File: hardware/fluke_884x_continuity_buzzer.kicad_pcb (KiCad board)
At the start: 4 copper layers, 67.4 x 71.4 mm, 70 parts, among them J2 Conn_01x02, J203 16 pin DIP socket, J204 16 pin DIP socket, J3 USB_B_Micro, P203 16 pin DIP plug, P204 16 pin DIP plug, U1 AZ117EH-3.3, U2 W25Q128JVS, U3 RP2040, Y1 ABLS-12.000MHZ-B4-T

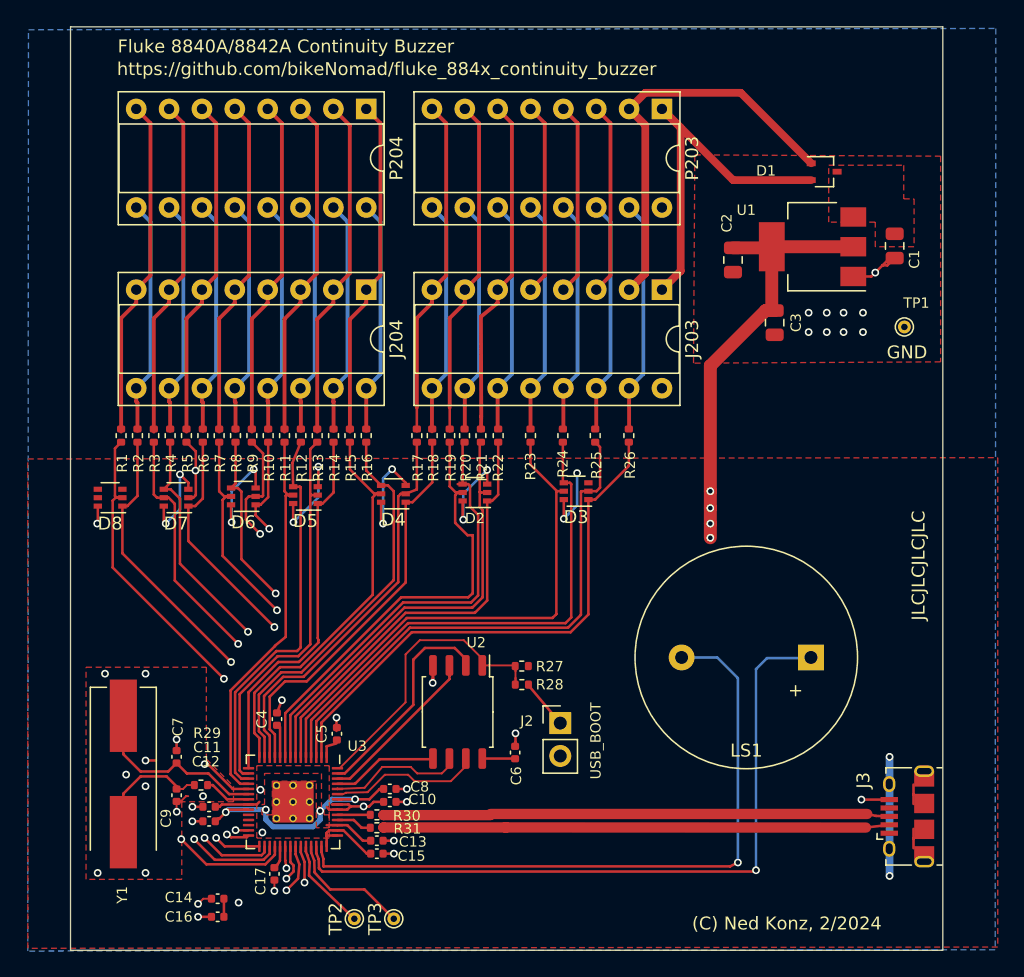
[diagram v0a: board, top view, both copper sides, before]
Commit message: WIP: made board shorter
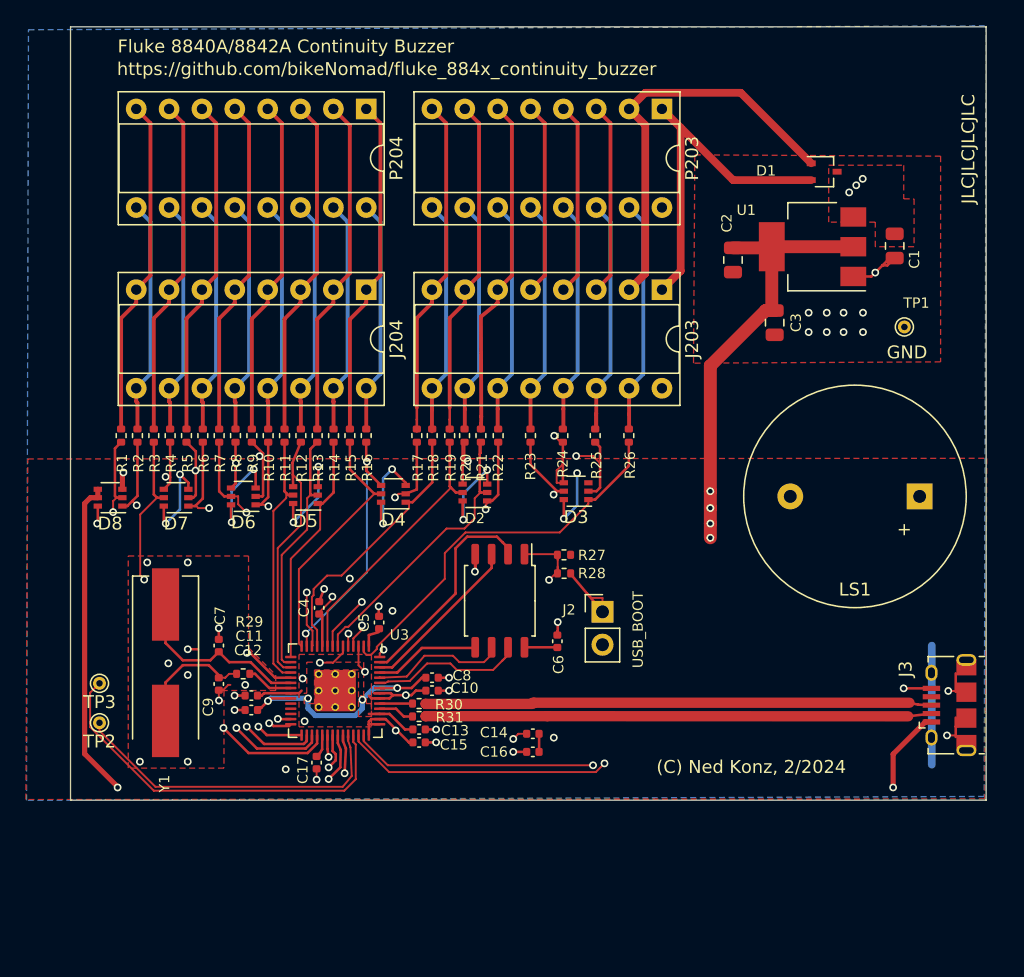
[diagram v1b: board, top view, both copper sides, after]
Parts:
- moved TP3 29.1 mm to (75.9, 76.2), turned to 180 degrees
- moved C14 27.5 mm to (109.4, 80.0)
- moved C16 27.5 mm to (109.4, 81.5)
- moved TP2 24.9 mm to (75.9, 79.2), turned to 180 degrees
- moved LS1 15.0 mm to (134.3, 61.7)
- moved C4 9.20 mm to (92.9, 70.3)
- moved Y1 9.20 mm to (81.0, 74.6)
- moved J2 9.20 mm to (114.8, 70.6)
- moved R29 9.20 mm to (87.0, 75.4)
- moved C10 9.20 mm to (101.6, 76.7)
- moved C11 9.20 mm to (87.6, 77.1)
- moved C12 9.20 mm to (87.6, 78.2)
- moved C13 9.20 mm to (100.6, 79.7)
- moved C15 9.20 mm to (100.6, 80.7)
- moved C17 9.20 mm to (92.7, 82.3)
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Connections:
- D8 pad 3: unconnected-(D8C-K-Pad3) -> Net-(D1-K)
- D8 pad 4: unconnected-(D8C-A-Pad4) -> /VBUS
- D8 pad 5: unconnected-(D8D-A-Pad5) -> /VBUS
- J3 pad 1: unconnected-(J3-VBUS-Pad1) -> /VBUS
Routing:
- net /VBUS: track 0.00 -> 91.5 mm, vias 0 -> 2
- net Net-(D1-K): track 0.00 -> 82.2 mm, vias 0 -> 4
- net /GPIO27_ADC1: track 9.70 -> 30.1 mm
- net /GPIO26_ADC0: track 7.09 -> 25.5 mm
- net RL4_3V: track 40.4 -> 27.2 mm, vias 0 -> 2
- net G1_3V: track 46.5 -> 33.4 mm
- net G7_3V: track 35.4 -> 22.3 mm
- net PDP_3V: track 31.0 -> 19.6 mm
- net G5_3V: track 34.0 -> 22.7 mm
- net RL3_3V: track 41.7 -> 30.4 mm
- net G3_3V: track 29.1 -> 18.1 mm
- net PS1_3V: track 30.1 -> 19.3 mm
- net PS2_3V: track 46.2 -> 35.4 mm
- net RL1_3V: track 34.4 -> 23.7 mm, vias 0 -> 2
- net RL2_3V: track 40.3 -> 29.7 mm, vias 0 -> 2
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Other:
- board size 67.4 x 71.4 mm -> 70.8 x 59.8 mm

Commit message: WIP: shortened board, added driver for keypad signals.
Also changed 30V R values.
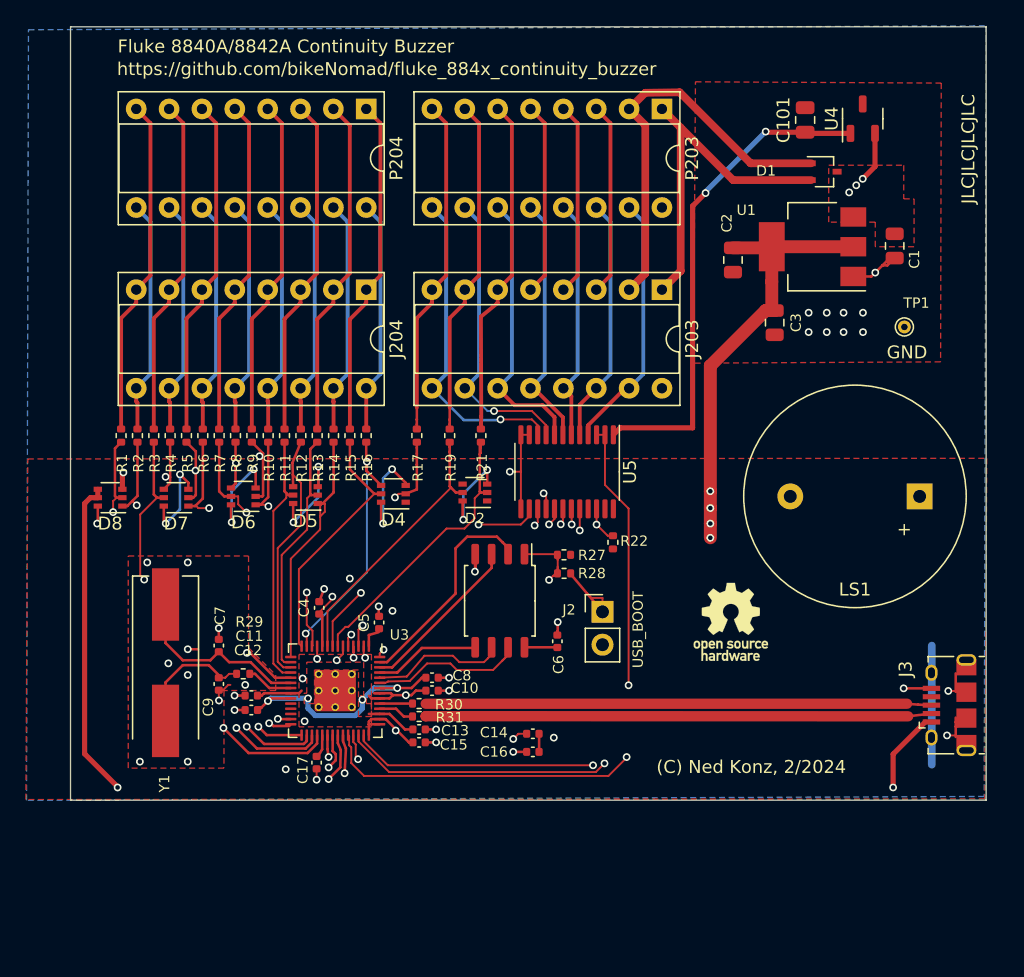
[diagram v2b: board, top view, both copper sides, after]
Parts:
- removed D3: BAT54CDW, Package_TO_SOT_SMD:SOT-363_SC-70-6
- removed R18, R20, R23, R24, R25, R26: 15k, Resistor_SMD:R_0402_1005Metric
- removed TP2, TP3: TestPoint, TestPoint:TestPoint_THTPad_D1.0mm_Drill0.5mm
- added C101: 10u, Capacitor_SMD:C_0805_2012Metric, F.Cu at (130.4, 32.6)
- added REF**: OSHW-Logo_5.7x6mm_SilkScreen, Symbol:OSHW-Logo_5.7x6mm_SilkScreen, F.Cu at (124.7, 71.4)
- added U4: umw_78l05_sot23, Package_TO_SOT_SMD:SOT-23-3, F.Cu at (134.9, 32.5)
- added U5: SN74LVC8T245PW, Package_SO:TSSOP-24_4.4x7.8mm_P0.65mm, F.Cu at (112.0, 59.8)
- R1, R10, R11, R12, R13, R14, R15, R16, R17, R19, R2, R21, R3, R4, R5, R6, R7, R8, R9: value 470k -> 270k
- R22: value 15k -> 10k
- moved R22 12.1 mm to (115.6, 65.2)
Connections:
- D2 pad 1: RL6_3V -> unconnected-(D2A-A-Pad1)
- D2 pad 4: RL1_3V -> unconnected-(D2C-A-Pad4)
- D4 pad 1: RL0_3V -> unconnected-(D4A-A-Pad1)
- R22 pad 1: /RL6 -> /GPIO27_ADC1
- R22 pad 2: RL6_3V -> +3V3
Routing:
- net +5V: track 0.00 -> 38.1 mm, vias 0 -> 2
- net /GPIO26_ADC0: track 25.5 -> 51.1 mm, vias 0 -> 2
- net RL5_3V: track 32.8 -> 22.3 mm
- net GND: track 57.2 -> 64.5 mm, vias 36 -> 37
- net RL2_3V: track 29.7 -> 22.9 mm
- net RL4_3V: track 27.2 -> 21.2 mm
- net RL3_3V: track 30.4 -> 24.6 mm, vias 0 -> 2
- net /RL0: track 19.7 -> 25.0 mm, vias 0 -> 1
- net Net-(D1-K): track 82.2 -> 86.1 mm
- net /RL1: track 19.7 -> 23.1 mm, vias 0 -> 1
- net +3V3: track 113.8 -> 110.9 mm, vias 25 -> 23
- net RL6_3V: track 27.4 -> 24.9 mm
- net /GPIO27_ADC1: track 30.1 -> 32.1 mm, vias 0 -> 2
- net /RL6: track 19.7 -> 21.6 mm
- net RL1_3V: track 23.7 -> 22.0 mm
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
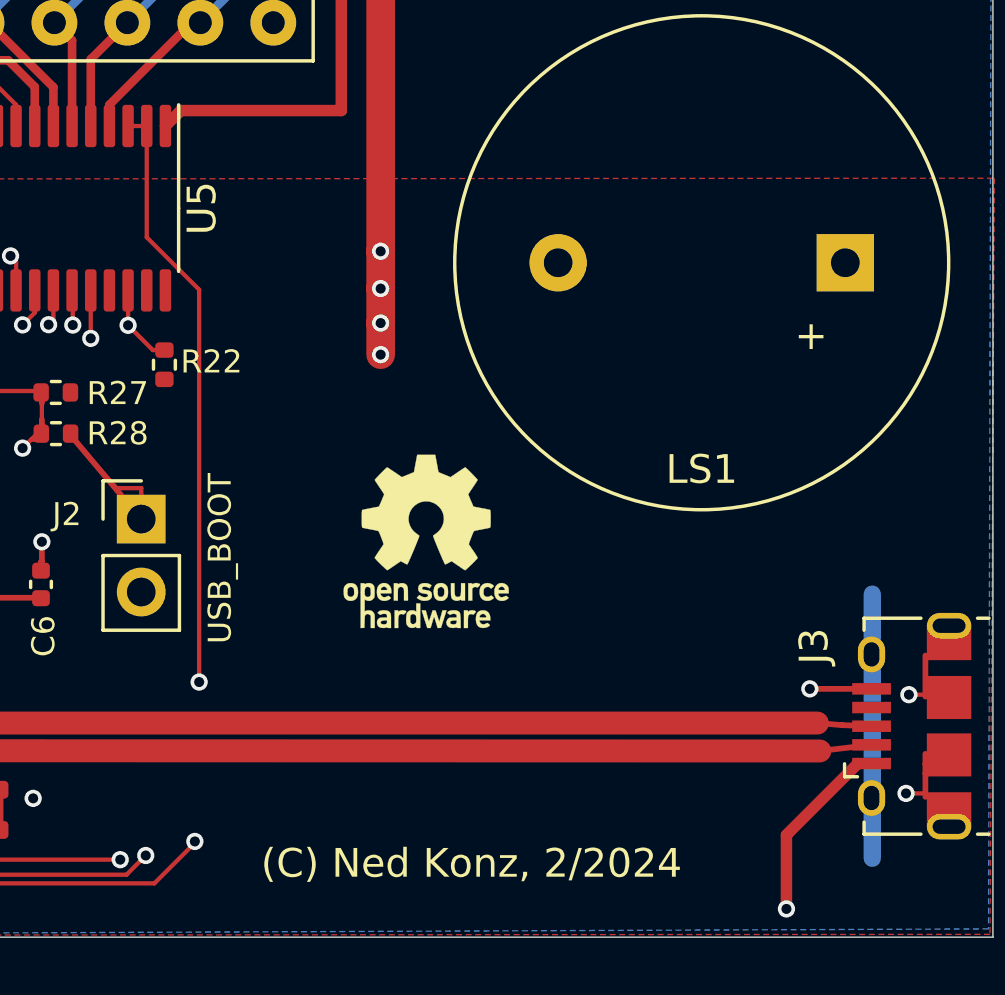
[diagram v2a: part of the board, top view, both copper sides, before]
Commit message: Added QR code; fixed JLC refs
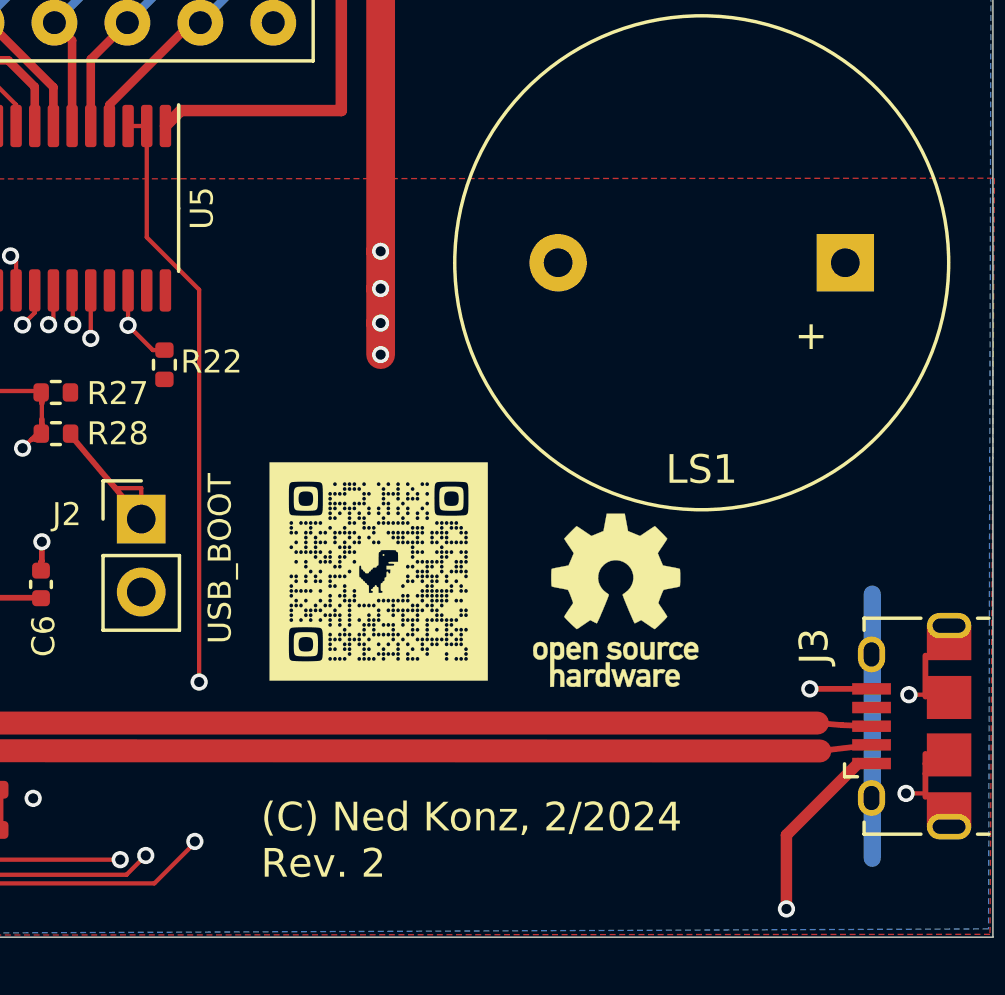
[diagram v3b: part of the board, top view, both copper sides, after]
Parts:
- added G***: LOGO, RP2040_minimal:qrcode, F.Cu at (123.0, 72.5)
- moved REF** 6.91 mm to (131.3, 73.5)
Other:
- board text added: "(C) Ned Konz, 2/2024 Rev. 2"
- board text removed: "(C) Ned Konz, 2/2024"

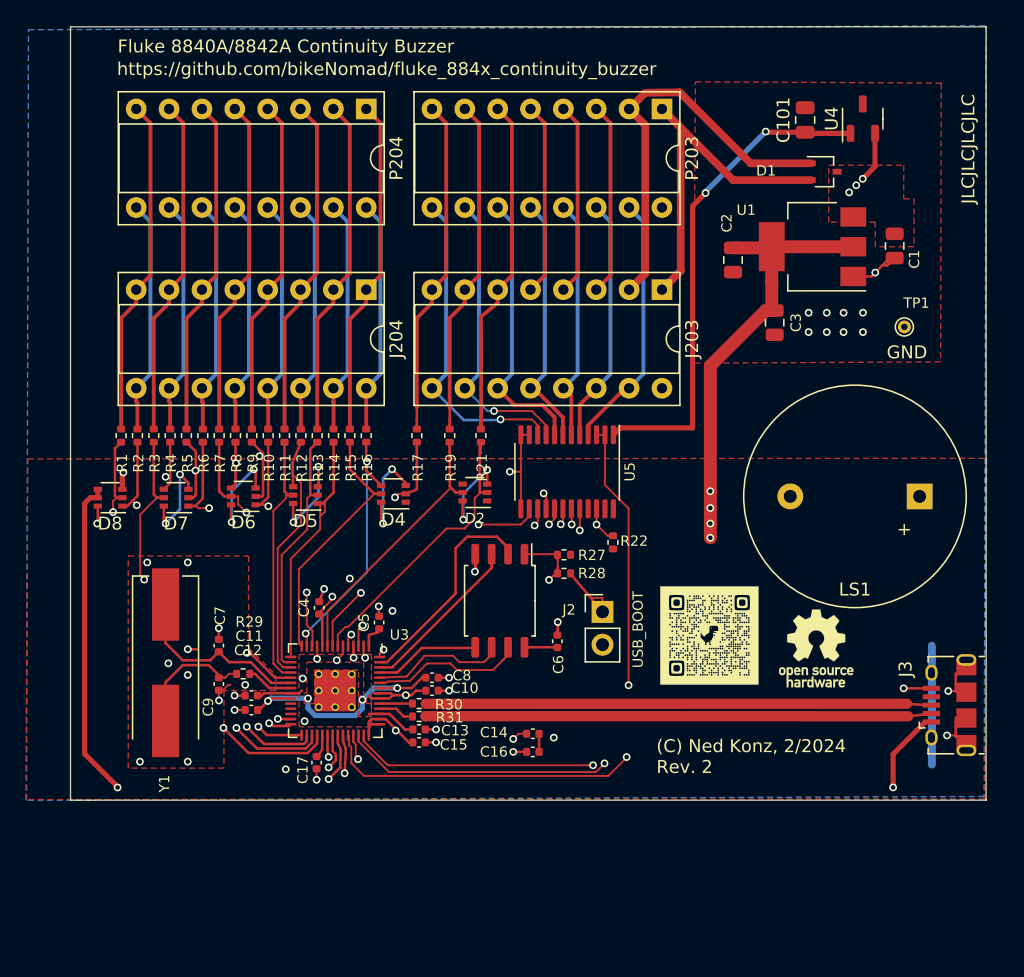
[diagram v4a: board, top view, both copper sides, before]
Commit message: Change R1-R19 to 200k
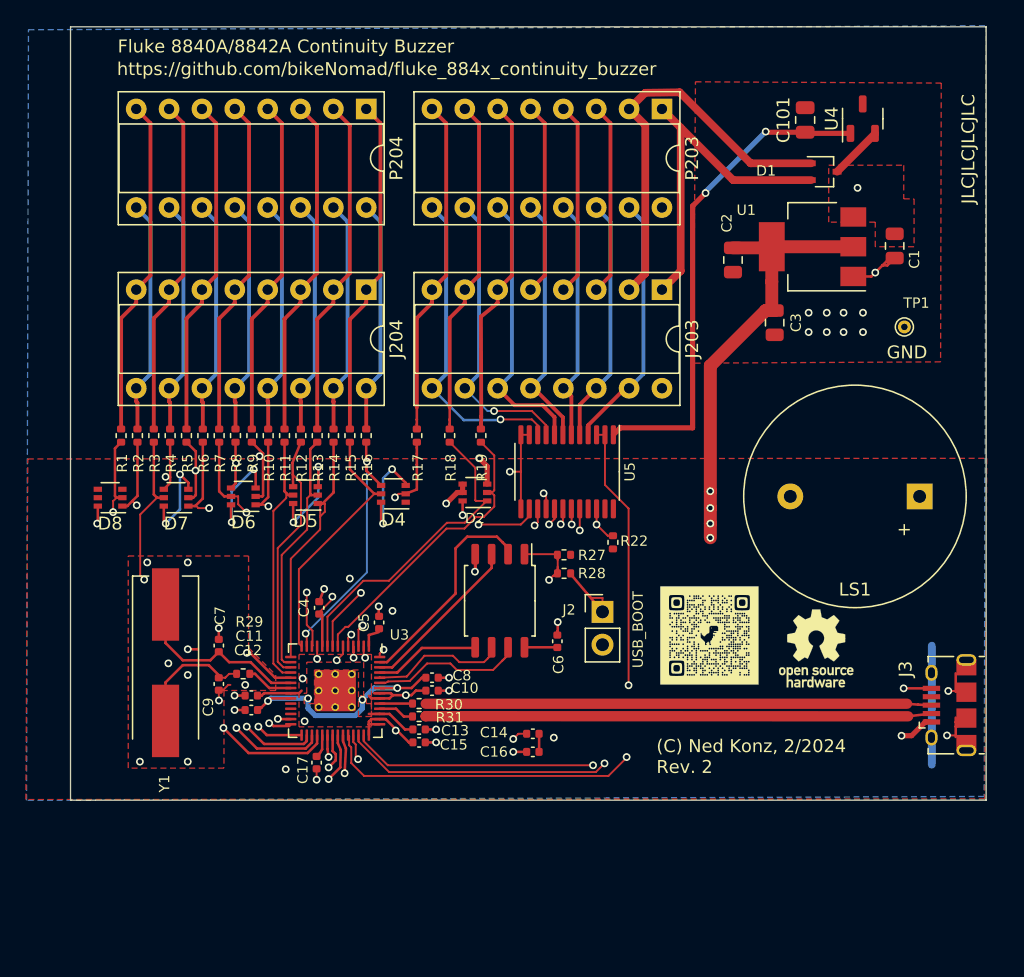
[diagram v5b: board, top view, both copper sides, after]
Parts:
- R1, R10, R11, R12, R13, R14, R15, R16, R17, R2, R3, R4, R5, R6, R7, R8, R9: value 270k -> 200k
- R18: renamed from R19; value 270k -> 200k
- R19: renamed from R21; value 270k -> 200k
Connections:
- D2 pad 1: unconnected-(D2A-A-Pad1) -> G7_3V
- D2 pad 3: +3V3 -> Net-(D1-K)
- D2 pad 4: unconnected-(D2C-A-Pad4) -> /VBUS
- D2 pad 5: G7_3V -> /VBUS
- D8 pad 3: Net-(D1-K) -> unconnected-(D8C-K-Pad3)
- D8 pad 4: /VBUS -> unconnected-(D8C-A-Pad4)
- D8 pad 5: /VBUS -> unconnected-(D8D-A-Pad5)
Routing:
- net /VBUS: track 91.0 -> 47.7 mm
- net Net-(D1-K): track 86.1 -> 45.5 mm, vias 4 -> 2
- net +3V3: track 110.9 -> 104.7 mm, vias 23 -> 22
- net G7_3V: track 21.9 -> 24.6 mm

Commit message: Removed bus buffer
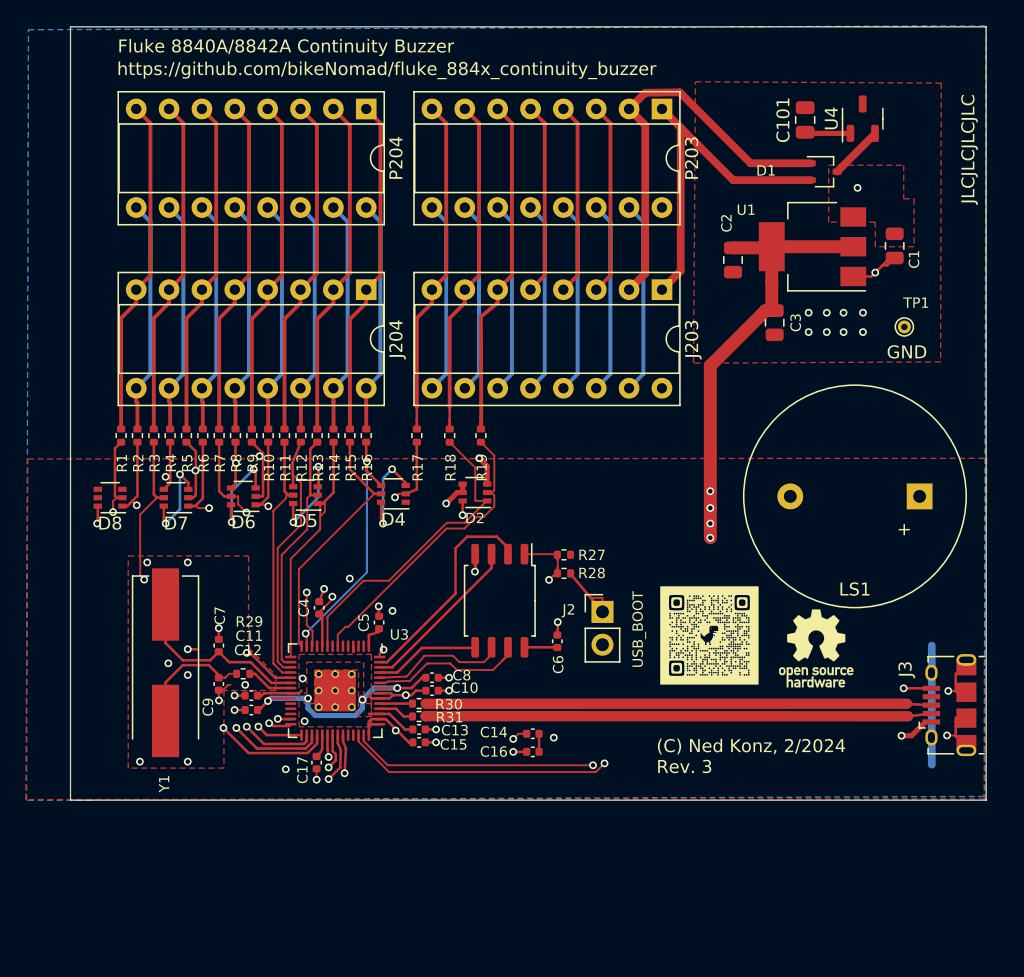
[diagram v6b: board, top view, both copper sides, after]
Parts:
- removed R22: 10k, Resistor_SMD:R_0402_1005Metric
- removed U5: SN74LVC8T245PW, Package_SO:TSSOP-24_4.4x7.8mm_P0.65mm
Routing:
- net /GPIO26_ADC0: track 51.1 -> 0.00 mm, vias 2 -> 0
- net +5V: track 38.1 -> 3.41 mm, vias 2 -> 0
- net /GPIO27_ADC1: track 32.1 -> 0.00 mm, vias 2 -> 0
- net RL6_3V: track 24.9 -> 0.00 mm, vias 2 -> 0
- net RL3_3V: track 24.6 -> 0.00 mm, vias 2 -> 0
- net RL5_3V: track 22.3 -> 0.00 mm, vias 2 -> 0
- net RL0_3V: track 22.2 -> 0.00 mm, vias 2 -> 0
- net RL1_3V: track 22.0 -> 0.00 mm, vias 2 -> 0
- net RL2_3V: track 22.9 -> 0.90 mm, vias 2 -> 0
- net RL4_3V: track 21.2 -> 0.00 mm, vias 2 -> 0
- net /RL0: track 25.0 -> 14.9 mm, vias 1 -> 0
- net /RL1: track 23.1 -> 14.9 mm, vias 1 -> 0
- net GND: track 64.5 -> 57.3 mm, vias 37 -> 36
- net /RL6: track 21.6 -> 14.9 mm
- net /RL3: track 19.7 -> 14.9 mm
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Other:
- board text added: "(C) Ned Konz, 2/2024 Rev. 3"
- board text removed: "(C) Ned Konz, 2/2024 Rev. 2"
